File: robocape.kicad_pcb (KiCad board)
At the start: 2 copper layers, 86.4 x 54.6 mm, 110 parts, among them J1 SMA, Q1 2N7002, SW1 SW_PUSH, U1 BEAGLEBONE, U10 MPU-9250, U11 MS5611-01BA, U2 CAT24C256W, U3 BQ32000, U4 XBee_Header, U5 PCA9685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

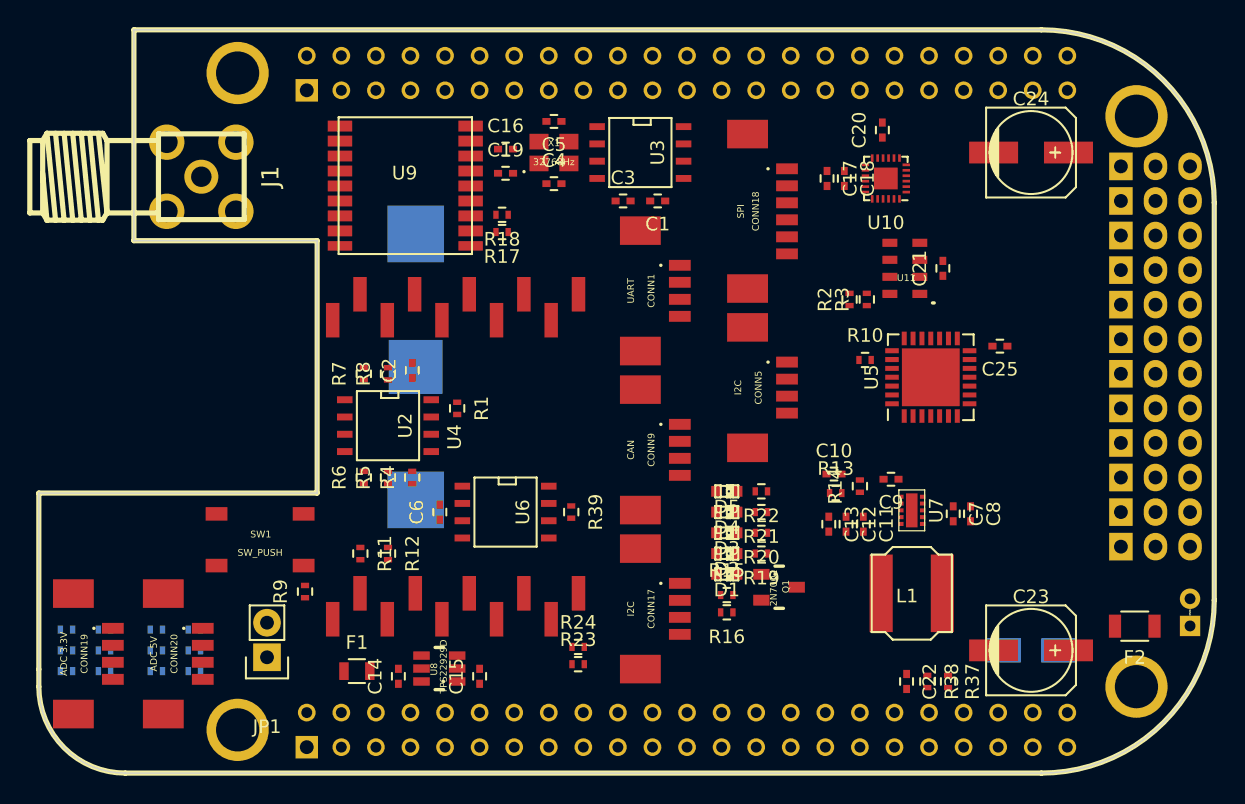
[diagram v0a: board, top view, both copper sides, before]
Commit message: PCB: Layout of close tracks
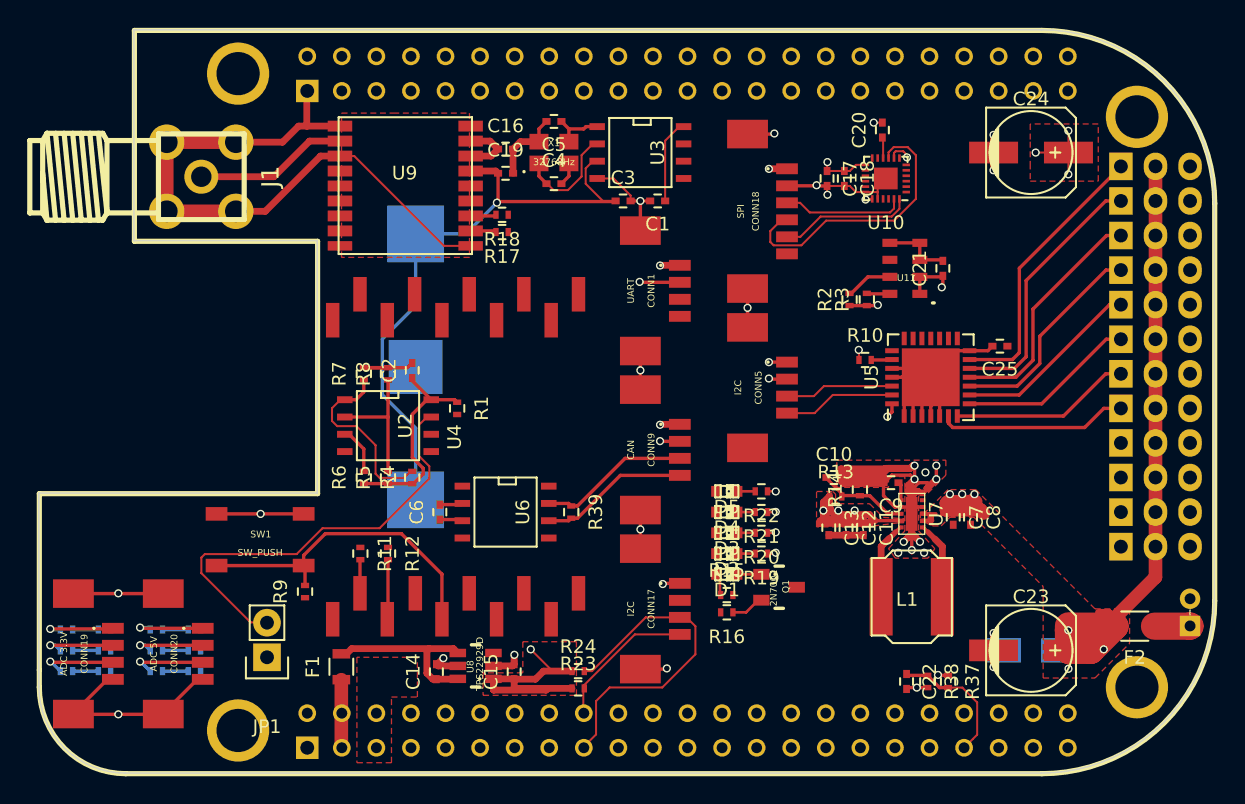
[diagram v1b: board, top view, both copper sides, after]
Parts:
- moved C14 2.81 mm to (102.9, 85.6)
- moved U8 2.67 mm to (107.1, 86.2)
- moved C15 2.56 mm to (108.6, 85.6)
- moved R24 1.78 mm to (113.3, 85.6)
- moved R23 1.78 mm to (113.3, 86.9)
- moved F1 1.19 mm to (95.9, 85.3), turned to 90 degrees
- moved C11 0.25 mm to (134.2, 75.1)
- moved C12 0.25 mm to (133.0, 75.1)
- moved C13 0.25 mm to (131.7, 75.1)
- moved C7 0.25 mm to (140.8, 74.3)
- moved C8 0.25 mm to (142.1, 74.3)
- moved L1 0.25 mm to (137.8, 80.1)
- moved R13 0.25 mm to (132.2, 72.8)
- moved R14 0.25 mm to (134.0, 72.3)
- moved C10 0.25 mm to (132.1, 71.4)
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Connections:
- CONN18 pad MECH: Net-(CONN18-PadMECH) -> GND
- CONN19 pad MECH: Net-(CONN19-PadMECH) -> GND
- CONN20 pad MECH: Net-(CONN20-PadMECH) -> GND
- U5 pad 29: (no net) -> GND
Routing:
- net GND: track 0.00 -> 340.2 mm, vias 0 -> 36
- net POWER: track 0.00 -> 124.2 mm, vias 0 -> 10
- net +5V: track 0.00 -> 74.1 mm, vias 0 -> 6
- net +3.3V_A: track 0.00 -> 57.3 mm, vias 0 -> 10
- net /Power/Back_Bat: track 0.00 -> 46.5 mm, vias 0 -> 1
- net Net-(JP1-Pad2): track 0.00 -> 32.0 mm
- net /Connectivity/I2C1_SCL: track 0.00 -> 24.6 mm
- net Net-(R9-Pad2): track 0.00 -> 24.0 mm
- net /Connectivity/PWM_11: track 0.00 -> 20.6 mm
- net /Sensors/MPU9250_MISO: track 0.00 -> 20.6 mm
- net /Connectivity/PWM_10: track 0.00 -> 19.5 mm
- net /Connectivity/PWM_9: track 0.00 -> 17.6 mm
- net /Connectivity/PWM_8: track 0.00 -> 15.8 mm
- net /Connectivity/PWM_4: track 0.00 -> 13.9 mm
- net /Connectivity/PWM_7: track 0.00 -> 13.9 mm
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- added copper zone on F.Cu, net +3.3V_A
- added copper zone on Power.Plane, net +3.3V_A
- added copper zone on F.Cu, net +5V
- added copper zone on Power.Plane, net +5V
- added copper zone on F.Cu, net GND
- added copper zone on Groun.Plane, net GND
- added copper zone on F.Cu, net POWER
- added copper zone on Power.Plane, net POWER
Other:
- copper layers 2 -> 4
- net class Default: clearance 0.2 -> 0.15; trace_width 0.25 -> 0.15
- rule trace_clearance: 0.2 -> 0.15
- rule trace_min: 0.1524 -> 0.15

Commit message: PCB: 3v3 zone fill in power plane + 3v3 wiring
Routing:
- net GND: track 340.2 -> 352.9 mm, vias 36 -> 39
- net +3V3: track 12.3 -> 16.9 mm, vias 0 -> 2
- net Net-(JP1-Pad2): track 32.0 -> 34.0 mm
- net +3.3V_A: track 57.3 -> 58.2 mm, vias 10 -> 11
- added copper zone on Power.Plane, net +3V3
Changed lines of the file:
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@@
   (general
     (links 323)
-    (no_connects 96)
+    (no_connects 74)
     (area 72.656559 38.184499 160.395501 93.475501)
     (thickness 1.6)
     (drawings 11)
-    (tracks 813)
+    (tracks 841)
     (zones 0)
     (modules 110)
@@
   (segment (start 105.384 48.856) (end 107.234 48.856) (width 0.5) (layer Front) (net 1) (status 30))
   (segment (start 107.234 48.856) (end 107.4 49.022) (width 0.5) (layer Front) (net 1) (status 30))
+  (segment (start 108.5 49.022) (end 108.5 48.099994) (width 0.5) (layer Front) (net 2))
+  (via (at 108.5 48.099994) (size 0.6) (drill 0.4) (layers Front Back) (net 2))
+  (segment (start 110.406 46.698) (end 110.698 46.698) (width 0.25) (layer Front) (net 2))
+  (segment (start 110.698 46.698) (end 112.298 48.298) (width 0.25) (layer Front) (net 2))
+  (segment (start 112.298 48.298) (end 112.606 48.298) (width 0.25) (layer Front) (net 2))
+  (segment (start 105.384 54.356) (end 106.744 54.356) (width 0.5) (layer Front) (net 2))
+  (segment (start 106.744 54.356) (end 106.8 54.3) (width 0.5) (layer Front) (net 2))
+  (via (at 106.8 54.3) (size 0.6) (drill 0.4) (layers Front Back) (net 2))
+  (segment (start 101.092 62.95) (end 101.75 62.95) (width 0.25) (layer Front) (net 2))
+  (segment (start 101.75 62.95) (end 101.8 63) (width 0.25) (layer Front) (net 2))
+  (via (at 101.8 63) (size 0.6) (drill 0.4) (layers Front Back) (net 2))
+  (segment (start 96.139 69.469) (end 96.139 72.661) (width 0.25) (layer Front) (net 2))
+  (segment (start 96.139 72.661) (end 94.754 74.046) (width 0.25) (layer Front) (net 2))
+  (segment (start 94.754 74.046) (end 93.116 74.046) (width 0.25) (layer Front) (net 2))
+  (segment (start 131.699 75.607) (end 132.969 75.607) (width 0.5) (layer Front) (net 2))
+  (segment (start 132.969 75.607) (end 134.239 75.607) (width 0.5) (layer Front) (net 2))
   (segment (start 136.995 73.541) (end 136.545 73.541) (width 0.25) (layer Front) (net 2))
   (segment (start 136.545 73.541) (end 135.721 72.717) (width 0.25) (layer Front) (net 2))
   (segment (start 135.721 72.717) (end 135.721 72.255) (width 0.25) (layer Front) (net 2))
   (segment (start 135.721 72.255) (end 135.721 71.755) (width 0.25) (layer Front) (net 2))
-  (segment (start 132.969 75.607) (end 134.239 75.607) (width 0.5) (layer Front) (net 2))
-  (segment (start 131.699 75.607) (end 132.969 75.607) (width 0.5) (layer Front) (net 2))
   (segment (start 138.16493 86.81) (end 137.514 86.81) (width 0.25) (layer Front) (net 2))
   (via (at 138.16493 86.81) (size 0.6) (drill 0.4) (layers Front Back) (net 2))
@@
   (segment (start 136.995 73.541) (end 137.445 73.541) (width 0.25) (layer Front) (net 2) (status 30))
   (segment (start 137.445 73.541) (end 137.795 73.891) (width 0.25) (layer Front) (net 2) (status 30))
+  (segment (start 104.394 65.844) (end 105.256 65.844) (width 0.25) (layer Front) (net 3))
+  (via (at 105.3 65.8) (size 0.6) (drill 0.4) (layers Front Back) (net 3))
+  (segment (start 105.256 65.844) (end 105.3 65.8) (width 0.25) (layer Front) (net 3))
   (segment (start 101.092 71.824) (end 101.192 71.824) (width 0.25) (layer Front) (net 3))
   (segment (start 101.192 71.824) (end 101.9 71.116) (width 0.25) (layer Front) (net 3))
@@
   (segment (start 112.606 46.698) (end 112.606 45.762) (width 0.25) (layer Front) (net 5) (status 10))
   (segment (start 112.606 45.762) (end 112.056 45.212) (width 0.25) (layer Front) (net 5) (status 20))
+  (segment (start 95.25 81.788) (end 95.25 80.176315) (width 0.5) (layer Front) (net 6))
+  (segment (start 95.25 80.176315) (end 95.25 79.65) (width 0.5) (layer Front) (net 6))
+  (segment (start 93.218 80.206) (end 95.220315 80.206) (width 0.25) (layer Front) (net 6))
+  (segment (start 95.220315 80.206) (end 95.25 80.176315) (width 0.25) (layer Front) (net 6))
+  (segment (start 95.25 79.65) (end 95.2 79.6) (width 0.5) (layer Front) (net 6))
+  (via (at 95.2 79.6) (size 0.6) (drill 0.4) (layers Front Back) (net 6))
+  (segment (start 107.4 47.244) (end 107.4 46.9) (width 0.5) (layer Front) (net 6))
+  (segment (start 107.4 46.9) (end 108 46.3) (width 0.5) (layer Front) (net 6))
+  (via (at 108 46.3) (size 0.6) (drill 0.4) (layers Front Back) (net 6))
   (segment (start 103.124 74.464) (end 104.69 74.464) (width 0.25) (layer Front) (net 6) (status 30))
   (segment (start 104.69 74.464) (end 104.775 74.549) (width 0.25) (layer Front) (net 6) (status 30))
@@
   (segment (start 106.812 46.656) (end 107.4 47.244) (width 0.5) (layer Front) (net 6) (status 20))
   (segment (start 95.885 88.646) (end 95.885 86.228) (width 1) (layer Front) (net 6) (status 30))
-  (segment (start 95.25 80.899) (end 95.25 81.788) (width 0.4) (layer Front) (net 6) (status 30))
   (segment (start 95.885 88.646) (end 95.885 91.186) (width 1) (layer Front) (net 6) (status 30))
   (segment (start 96.078 88.453) (end 95.885 88.646) (width 0.5) (layer Front) (net 6) (status 30))
@@
   (segment (start 90.932 49.276) (end 93.552 46.656) (width 0.5) (layer Front) (net 53))
   (segment (start 93.552 46.656) (end 95.784 46.656) (width 0.5) (layer Front) (net 53) (status 20))
+  (segment (start 104.394 66.744) (end 104.338 66.8) (width 0.15) (layer Front) (net 54))
+  (segment (start 104.338 66.8) (end 102.618 66.8) (width 0.15) (layer Front) (net 54))
+  (segment (start 102.618 66.8) (end 102.489 66.929) (width 0.15) (layer Front) (net 54))
   (segment (start 90.424 82.042) (end 90.4 82.018) (width 0.15) (layer Front) (net 54))
   (segment (start 90.4 82.018) (end 89.218 82.018) (width 0.15) (layer Front) (net 54))
@@
       )
     )
+  )
+  (zone (net 6) (net_name +3V3) (layer Power.Plane) (hatch edge 0.508)
+    (connect_pads (clearance 0.3))
+    (min_thickness 0.1)
+    (fill yes (arc_segments 16) (thermal_gap 0.3) (thermal_bridge_width 0.5) (smoothing fillet) (radius 0.2))
+    (polygon
+      (pts
+        (xy 96.8 92.3) (xy 96.8 84.6) (xy 96.8 84.3) (xy 96.8 83.8) (xy 98.8 83.8)
+        (xy 98.8 56) (xy 98.8 55.5) (xy 109.2 55.5) (xy 109.2 44.3) (xy 94.2 44.3)
+        (xy 94.2 86.1) (xy 94.2 87) (xy 94.7 87.5) (xy 94.9 87.7) (xy 94.9 92.3)
+      )
+    )

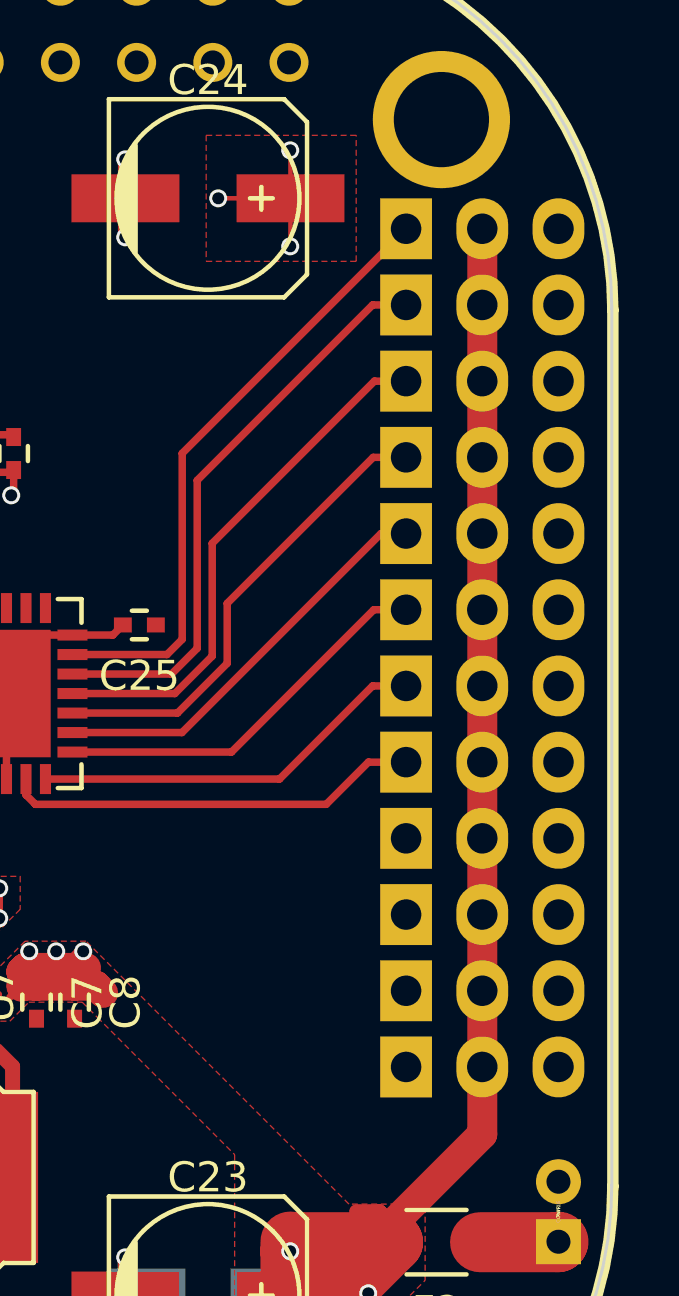
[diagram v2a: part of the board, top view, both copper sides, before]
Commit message: PCB: PWM silkscreen & some 3d models
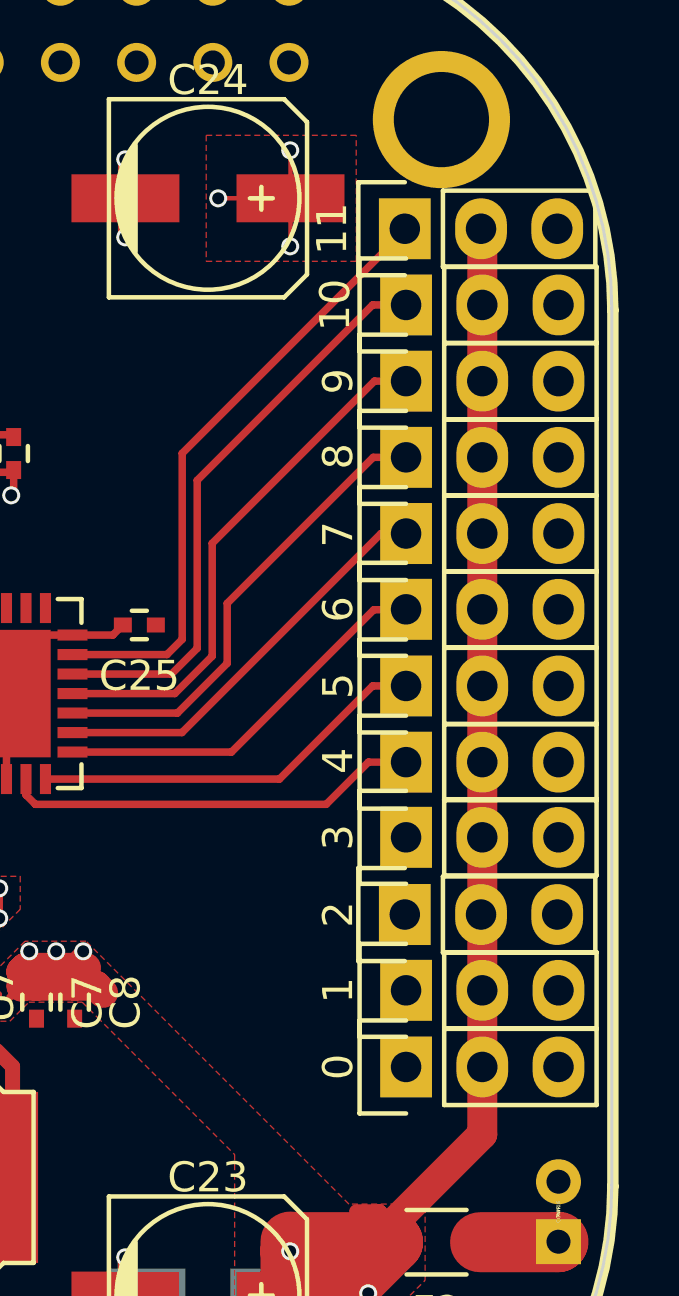
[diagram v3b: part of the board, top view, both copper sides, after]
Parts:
- 0: renamed from CONN2; moved to F.Cu
- 1: renamed from CONN3; moved to F.Cu
- 10: renamed from CONN14; moved to F.Cu
- 11: renamed from CONN15; moved to F.Cu
- 2: renamed from CONN4; moved to F.Cu
- 3: renamed from CONN6; moved to F.Cu
- 4: renamed from CONN7; moved to F.Cu
- 5: renamed from CONN8; moved to F.Cu
- 6: renamed from CONN10; moved to F.Cu
- 7: renamed from CONN11; moved to F.Cu
- 8: renamed from CONN12; moved to F.Cu
- 9: renamed from CONN13; moved to F.Cu
- turned 11 to 90 degrees
- turned 2 to 90 degrees
- turned 3 to 90 degrees
- turned 1 to 90 degrees
- turned 6 to 90 degrees
- turned 0 to 90 degrees
- turned 10 to 90 degrees
- turned 4 to 90 degrees
- turned 5 to 90 degrees
- turned 7 to 90 degrees
- turned 8 to 90 degrees
- turned 9 to 90 degrees

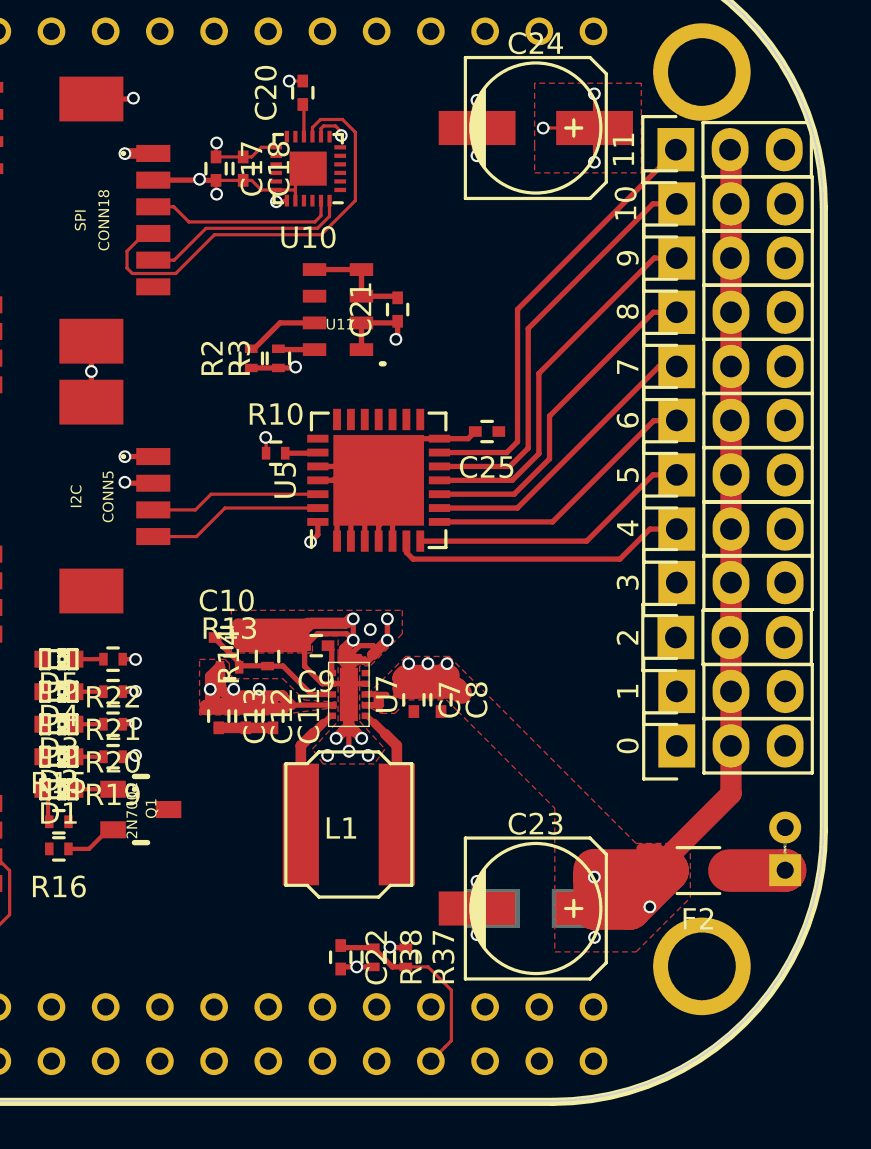
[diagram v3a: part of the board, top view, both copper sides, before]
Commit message: PCB: Correct footprint and layout of 5V regulator
Also added some 3D models (GPS, SMA)
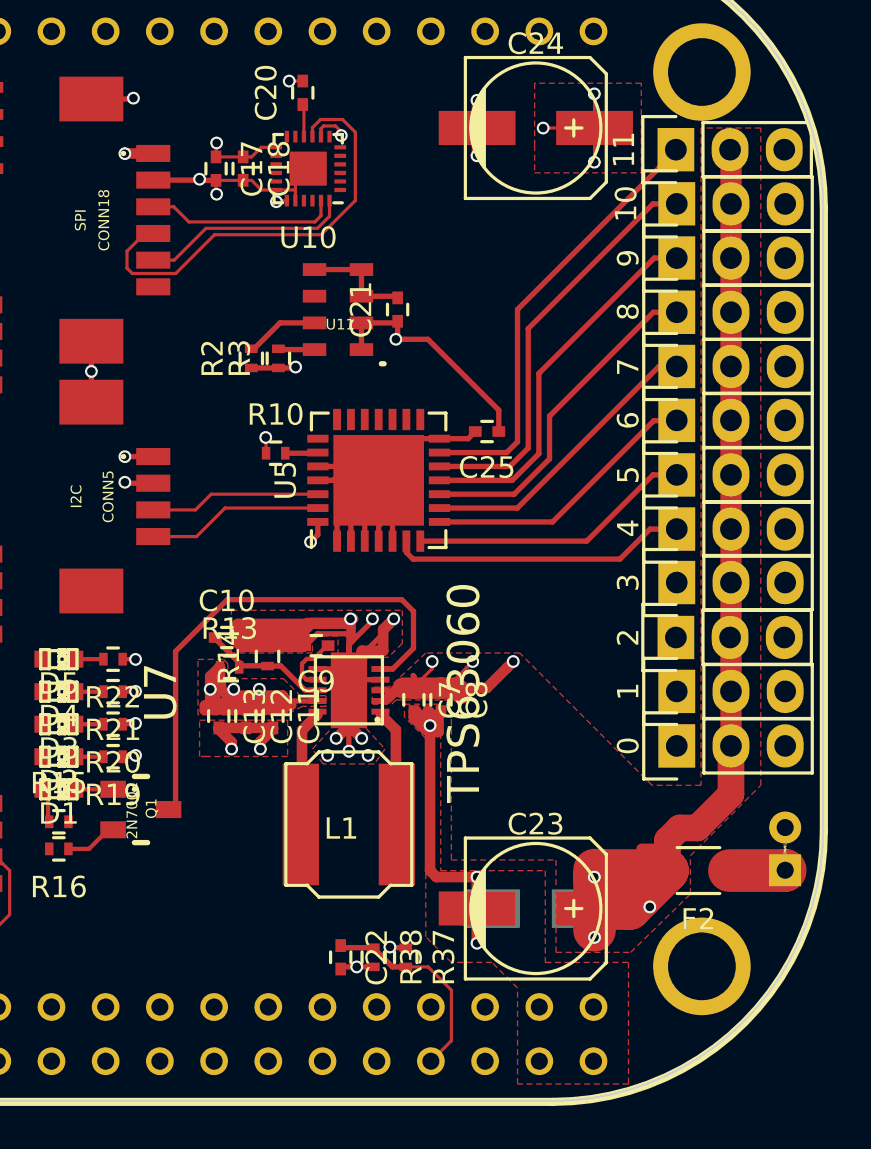
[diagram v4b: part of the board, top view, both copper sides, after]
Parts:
- U7: footprint _std:WSON10 -> _std:SON-10
- moved U7 0.09 mm to (137.8, 74.0), turned to 270 degrees
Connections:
- U5 pad 29: GND -> (no net)
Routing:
- net /Power/PWR_GOOD: track 0.00 -> 23.8 mm
- net GND: track 352.9 -> 375.5 mm, vias 39 -> 40
- net +3.3V_A: track 58.2 -> 65.4 mm
- net Net-(C9-Pad1): track 1.36 -> 2.92 mm
- net Net-(C10-Pad1): track 6.79 -> 6.04 mm
- net POWER: track 124.2 -> 123.6 mm
